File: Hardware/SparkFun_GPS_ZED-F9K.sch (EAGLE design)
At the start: 73 parts, among them J3 QWIIC_RIGHT_ANGLE, J4 QWIIC_RIGHT_ANGLE, U1 DUAL-OPTO_HCPL-073L, U2 U-BLOX_ZED_F9R, U3 UHS_INVERTER_SCHMITT_TRIGGERS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, U4 UHS_INVERTER_SCHMITT_TRIGGERS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, U5 3.3V

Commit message: Updates libraries, replaces F9R with F9K, fixes some text in schematic, deletes blank sheets in schematic
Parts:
- FB1: value 120NH -> 120Ω; device SparkFun-Coils:FERRITE_BEAD_GNSS -> SparkFun-Coils:FERRITE_BEAD-120_OHM-0402
- U1: value DUAL-OPTO_HCPL-073L -> DUAL-OPTO_HCPL-073LSOIC-8; device SparkFun-DiscreteSemi:DUAL-OPTO_HCPL-073L -> SparkFun-DiscreteSemi:DUAL-OPTO_HCPL-073LSOIC-8
- U2: value U-BLOX_ZED_F9R -> U-BLOX_ZED_F9K; device SparkFun-GPS:U-BLOX_ZED_F9R -> f9k:U-BLOX_ZED_F9K
- renumbered JP1 to PWR, JP2 to PPS, JP3 to RTK, JP4 to GEO, JP5 to SPI
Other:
- note added: "GNSS/Dead Reckoning Module - ublox ZED-F9K"
- note removed: "Dead Reckoning Module - ublox ZED-F9R"
- moved on the sheet: C1, C6, C7, R4, R7

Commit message: Updates script being used
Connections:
- net DIR_SCHMITT renamed DIR_INV
- net WT_SCHMITT renamed WT_INV
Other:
- moved on the sheet: C7
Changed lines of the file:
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@@
 <attribute name="VALUE" x="76.2" y="81.534" size="1.778" layer="96" font="vector" align="bottom-center"/>
 </instance>
-<instance part="GND26" gate="1" x="76.2" y="30.48" smashed="yes">
-<attribute name="VALUE" x="76.2" y="30.226" size="1.778" layer="96" font="vector" align="top-center"/>
+<instance part="GND26" gate="1" x="78.74" y="30.48" smashed="yes">
+<attribute name="VALUE" x="78.74" y="30.226" size="1.778" layer="96" font="vector" align="top-center"/>
 </instance>
 <instance part="D1" gate="G$1" x="43.18" y="45.72" smashed="yes" rot="R90">
@@
 <attribute name="VALUE" x="69.85" y="61.341" size="1.778" layer="96" font="vector"/>
 </instance>
-<instance part="C7" gate="G$1" x="76.2" y="40.64" smashed="yes">
-<attribute name="NAME" x="71.374" y="43.561" size="1.778" layer="95" font="vector"/>
-<attribute name="VALUE" x="69.088" y="38.481" size="1.778" layer="96" font="vector"/>
+<instance part="C7" gate="G$1" x="78.74" y="40.64" smashed="yes">
+<attribute name="NAME" x="73.914" y="43.561" size="1.778" layer="95" font="vector"/>
+<attribute name="VALUE" x="71.628" y="38.481" size="1.778" layer="96" font="vector"/>
 </instance>
 <instance part="GND29" gate="1" x="76.2" y="53.34" smashed="yes">
@@
 </segment>
 <segment>
-<wire x1="76.2" y1="38.1" x2="76.2" y2="35.56" width="0.1524" layer="91"/>
-<wire x1="76.2" y1="35.56" x2="76.2" y2="33.02" width="0.1524" layer="91"/>
+<wire x1="78.74" y1="38.1" x2="78.74" y2="35.56" width="0.1524" layer="91"/>
+<wire x1="78.74" y1="35.56" x2="78.74" y2="33.02" width="0.1524" layer="91"/>
 <wire x1="88.9" y1="38.1" x2="88.9" y2="35.56" width="0.1524" layer="91"/>
-<wire x1="88.9" y1="35.56" x2="76.2" y2="35.56" width="0.1524" layer="91"/>
-<junction x="76.2" y="35.56"/>
+<wire x1="88.9" y1="35.56" x2="78.74" y2="35.56" width="0.1524" layer="91"/>
+<junction x="78.74" y="35.56"/>
 <pinref part="GND26" gate="1" pin="GND"/>
 <pinref part="C7" gate="G$1" pin="2"/>
@@
 </segment>
 <segment>
-<wire x1="88.9" y1="71.12" x2="76.2" y2="71.12" width="0.1524" layer="91"/>
-<junction x="88.9" y="71.12"/>
+<wire x1="93.98" y1="71.12" x2="81.28" y2="71.12" width="0.1524" layer="91"/>
+<wire x1="81.28" y1="71.12" x2="76.2" y2="71.12" width="0.1524" layer="91"/>
 <wire x1="76.2" y1="71.12" x2="76.2" y2="68.58" width="0.1524" layer="91"/>
-<wire x1="88.9" y1="48.26" x2="88.9" y2="71.12" width="0.1524" layer="91"/>
-<junction x="88.9" y="71.12"/>
-<wire x1="76.2" y1="45.72" x2="76.2" y2="48.26" width="0.1524" layer="91"/>
-<wire x1="76.2" y1="48.26" x2="88.9" y2="48.26" width="0.1524" layer="91"/>
+<wire x1="78.74" y1="45.72" x2="78.74" y2="48.26" width="0.1524" layer="91"/>
+<wire x1="78.74" y1="48.26" x2="81.28" y2="48.26" width="0.1524" layer="91"/>
 <pinref part="SUPPLY22" gate="G$1" pin="3.3V"/>
 <pinref part="C6" gate="G$1" pin="1"/>
 <pinref part="C7" gate="G$1" pin="1"/>
 <pinref part="U3" gate="U1" pin="VCC"/>
-<wire x1="93.98" y1="71.12" x2="88.9" y2="71.12" width="0.1524" layer="91"/>
+<wire x1="81.28" y1="48.26" x2="93.98" y2="48.26" width="0.1524" layer="91"/>
 <wire x1="76.2" y1="78.74" x2="76.2" y2="71.12" width="0.1524" layer="91"/>
 <junction x="76.2" y="71.12"/>
 <pinref part="U4" gate="U1" pin="VCC"/>
-<wire x1="93.98" y1="48.26" x2="88.9" y2="48.26" width="0.1524" layer="91"/>
-<junction x="88.9" y="48.26"/>
+<wire x1="81.28" y1="48.26" x2="81.28" y2="71.12" width="0.1524" layer="91"/>
+<junction x="81.28" y="48.26"/>
+<junction x="81.28" y="71.12"/>
 </segment>
 <segment>
@@
 </segment>
 </net>
-<net name="WT_SCHMITT" class="0">
+<net name="WT_INV" class="0">
 <segment>
 <pinref part="R7" gate="G$1" pin="1"/>
@@
 </segment>
 </net>
-<net name="DIR_SCHMITT" class="0">
+<net name="DIR_INV" class="0">
 <segment>
 <pinref part="R4" gate="G$1" pin="1"/>

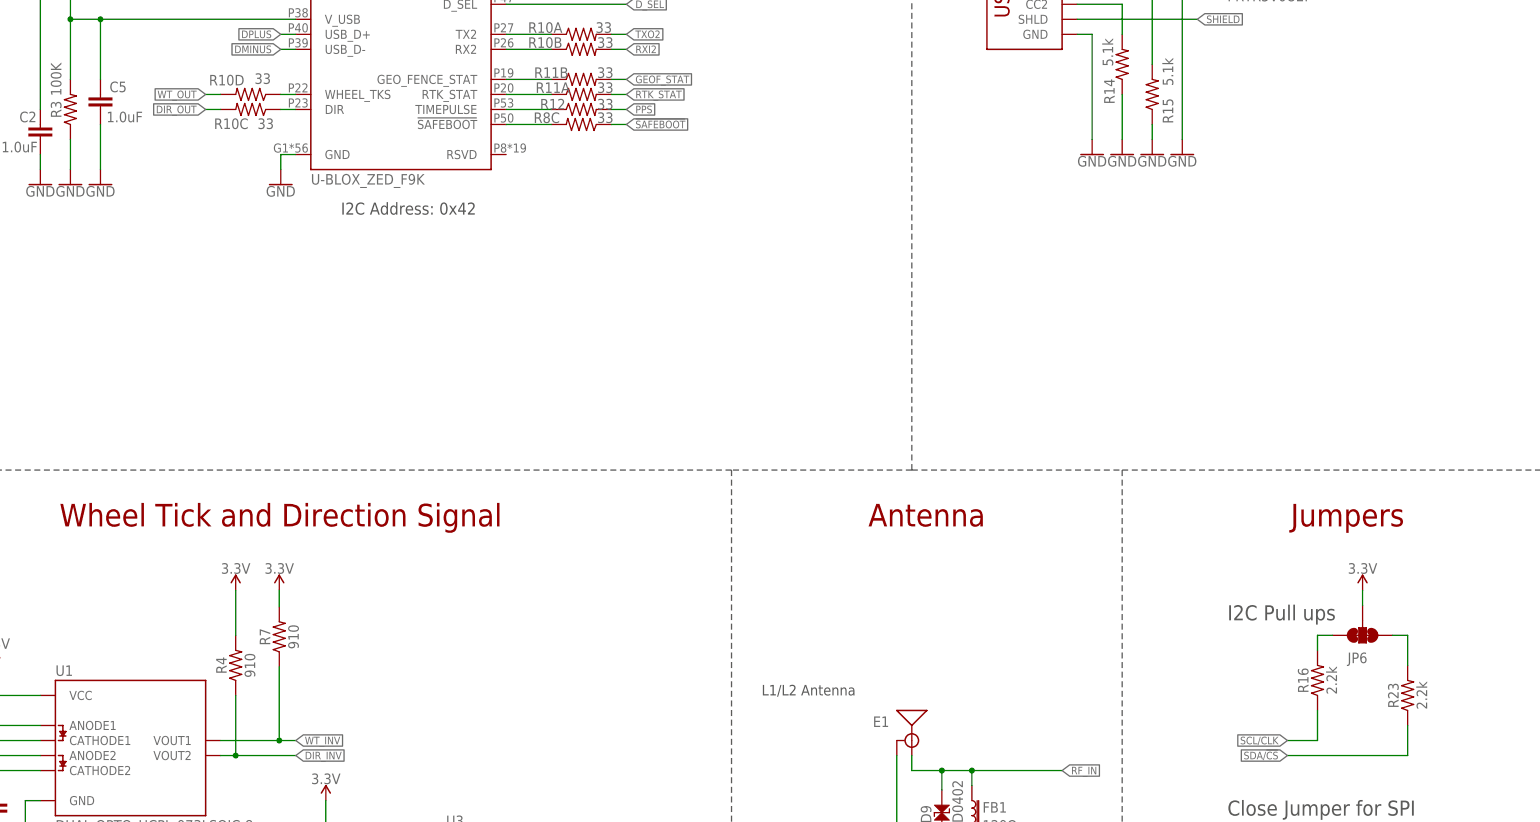
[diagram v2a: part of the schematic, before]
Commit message: Moves traces for better ground pour and to reduce cross talk
* Replaces all capacitors with smaller footprint
* Replaces 2.2K resistors with 4.7K resistors
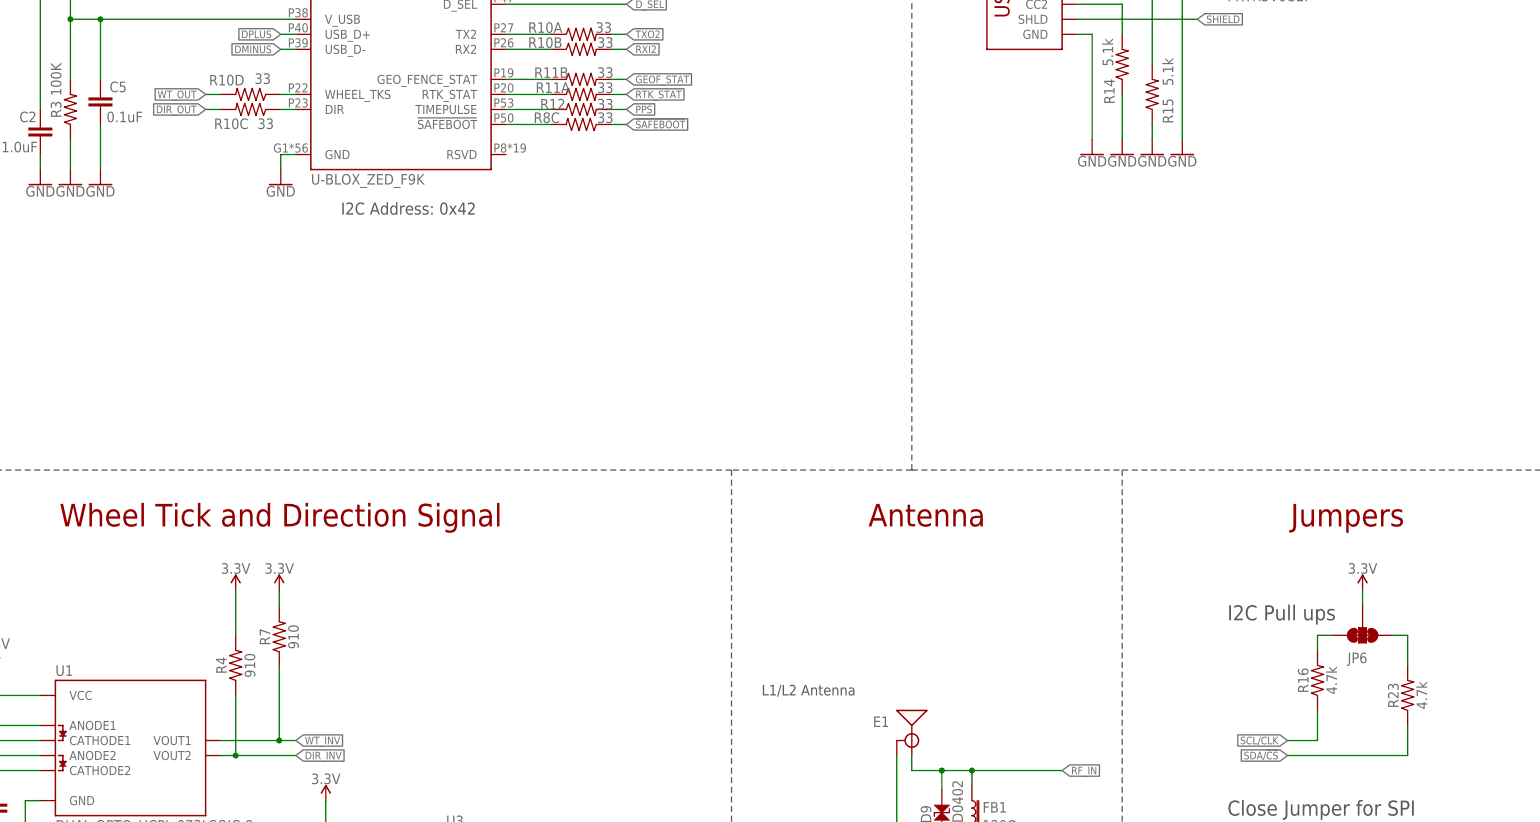
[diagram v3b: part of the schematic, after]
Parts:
- C1, C6, C7: device SparkFun-Capacitors:0.1UF-0402-10V-10%-X7R -> SparkFun-Capacitors:0.1UF-0402T-6.3V-10%-X7R
- C10, C2, C9: device SparkFun-Capacitors:1.0UF-0603-16V-10%-X7R -> SparkFun-Capacitors:1.0UF-0402T-16V-10%
- C5: value 1.0uF -> 0.1uF; device SparkFun-Capacitors:1.0UF-0603-16V-10%-X7R -> SparkFun-Capacitors:0.1UF-0402T-6.3V-10%-X7R
- R16, R23: value 2.2k -> 4.7k; device SparkFun-Resistors:2.2KOHM-0603-1/10W-1% -> SparkFun-Resistors:4.7KOHM-0402T-1/16W-1%
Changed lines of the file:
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@@
 <?xml version="1.0" encoding="utf-8"?>
 <!DOCTYPE eagle SYSTEM "eagle.dtd">
-<eagle version="9.6.2">
+<eagle version="9.5.1">
 <drawing>
 <settings>
@@
 <parts>
 <part name="J3" library="SparkFun-Connectors" deviceset="QWIIC_CONNECTOR" device="JS-1MM" value="QWIIC_RIGHT_ANGLE"/>
-<part name="R23" library="SparkFun-Resistors" deviceset="2.2KOHM" device="-0603-1/10W-1%" value="2.2k"/>
-<part name="R16" library="SparkFun-Resistors" deviceset="2.2KOHM" device="-0603-1/10W-1%" value="2.2k"/>
+<part name="R23" library="SparkFun-Resistors" deviceset="4.7KOHM" device="-0402T-1/16W-1%" value="4.7k"/>
+<part name="R16" library="SparkFun-Resistors" deviceset="4.7KOHM" device="-0402T-1/16W-1%" value="4.7k"/>
 <part name="JP6" library="SparkFun-Jumpers" deviceset="JUMPER-SMT_3_2-NC_TRACE" device="_SILK" package3d_urn="urn:adsk.eagle:package:39289/1"/>
 <part name="GND12" library="SparkFun-PowerSymbols" deviceset="GND" device=""/>
@@
 <part name="GND15" library="SparkFun-PowerSymbols" deviceset="GND" device=""/>
 <part name="SUPPLY11" library="SparkFun-PowerSymbols" deviceset="3.3V" device=""/>
-<part name="C9" library="SparkFun-Capacitors" deviceset="1.0UF" device="-0603-16V-10%-X7R" value="1.0uF"/>
-<part name="C10" library="SparkFun-Capacitors" deviceset="1.0UF" device="-0603-16V-10%-X7R" value="1.0uF"/>
+<part name="C9" library="SparkFun-Capacitors" deviceset="1.0UF" device="-0402T-16V-10%" value="1.0uF"/>
+<part name="C10" library="SparkFun-Capacitors" deviceset="1.0UF" device="-0402T-16V-10%" value="1.0uF"/>
 <part name="GND14" library="SparkFun-PowerSymbols" deviceset="GND" device=""/>
 <part name="GND17" library="SparkFun-PowerSymbols" deviceset="GND" device=""/>
@@
 <part name="SUPPLY1" library="SparkFun-PowerSymbols" deviceset="V_BATT" device=""/>
 <part name="U2" library="f9k" deviceset="U-BLOX_ZED_F9K" device=""/>
-<part name="C2" library="SparkFun-Capacitors" deviceset="1.0UF" device="-0603-16V-10%-X7R" value="1.0uF"/>
+<part name="C2" library="SparkFun-Capacitors" deviceset="1.0UF" device="-0402T-16V-10%" value="1.0uF"/>
 <part name="SUPPLY3" library="SparkFun-PowerSymbols" deviceset="3.3V" device=""/>
 <part name="R3" library="SparkFun-Resistors" deviceset="100KOHM" device="-0402-1/16W-1%" value="100K"/>
@@
 <part name="R4" library="SparkFun-Resistors" deviceset="910OHM" device="-0603-1/10W-5%" value="910"/>
 <part name="U1" library="SparkFun-DiscreteSemi" deviceset="DUAL-OPTO_HCPL-073L" device="SOIC-8"/>
-<part name="C1" library="SparkFun-Capacitors" deviceset="0.1UF" device="-0402-10V-10%-X7R" value="0.1uF"/>
+<part name="C1" library="SparkFun-Capacitors" deviceset="0.1UF" device="-0402T-6.3V-10%-X7R" value="0.1uF"/>
 <part name="SUPPLY21" library="SparkFun-PowerSymbols" deviceset="3.3V" device=""/>
 <part name="GND25" library="SparkFun-PowerSymbols" deviceset="GND" device=""/>
@@
 <part name="SUPPLY23" library="SparkFun-PowerSymbols" deviceset="3.3V" device=""/>
 <part name="SUPPLY24" library="SparkFun-PowerSymbols" deviceset="3.3V" device=""/>
-<part name="C6" library="SparkFun-Capacitors" deviceset="0.1UF" device="-0402-10V-10%-X7R" value="0.1uF"/>
-<part name="C7" library="SparkFun-Capacitors" deviceset="0.1UF" device="-0402-10V-10%-X7R" value="0.1uF"/>
+<part name="C6" library="SparkFun-Capacitors" deviceset="0.1UF" device="-0402T-6.3V-10%-X7R" value="0.1uF"/>
+<part name="C7" library="SparkFun-Capacitors" deviceset="0.1UF" device="-0402T-6.3V-10%-X7R" value="0.1uF"/>
 <part name="GND29" library="SparkFun-PowerSymbols" deviceset="GND" device=""/>
-<part name="C5" library="SparkFun-Capacitors" deviceset="1.0UF" device="-0603-16V-10%-X7R" value="1.0uF"/>
+<part name="C5" library="SparkFun-Capacitors" deviceset="0.1UF" device="-0402T-6.3V-10%-X7R" value="0.1uF"/>
 <part name="GND20" library="SparkFun-PowerSymbols" deviceset="GND" device=""/>
 <part name="GND21" library="SparkFun-PowerSymbols" deviceset="GND" device=""/>

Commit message: Flips FTDI header, adds testpoint for VBAT, fixes dimension line width
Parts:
- added TP1: TEST-POINT3X5, SparkFun-Connectors:TEST-POINT3X5
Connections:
- net GND: now also J7.6; no longer J7.1
- net RXI2: now also J7.3; no longer J7.4
- net TXO2: now also J7.2; no longer J7.5
- net V_BATT: now also TP1.1
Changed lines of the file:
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@@
 <?xml version="1.0" encoding="utf-8"?>
 <!DOCTYPE eagle SYSTEM "eagle.dtd">
-<eagle version="9.5.1">
+<eagle version="9.6.2">
 <drawing>
 <settings>
@@
 <part name="U3" library="SparkFun-IC-Amplifiers" deviceset="UHS_INVERTER_SCHMITT_TRIGGER" device="SIP6" value="UHS_INVERTER_SCHMITT_TRIGGERSIP6"/>
 <part name="U4" library="SparkFun-IC-Amplifiers" deviceset="UHS_INVERTER_SCHMITT_TRIGGER" device="SIP6" value="UHS_INVERTER_SCHMITT_TRIGGERSIP6"/>
+<part name="TP1" library="SparkFun-Connectors" deviceset="TEST-POINT" device="3X5"/>
 </parts>
 <sheets>
@@
 <attribute name="VALUE" x="96.52" y="33.02" size="1.778" layer="95"/>
 </instance>
+<instance part="TP1" gate="G$1" x="391.16" y="208.28" smashed="yes">
+<attribute name="NAME" x="391.16" y="210.82" size="1.778" layer="95" font="vector"/>
+</instance>
 </instances>
 <busses>
@@
 </segment>
 <segment>
-<pinref part="J7" gate="G$1" pin="1"/>
-<wire x1="391.16" y1="86.36" x2="393.7" y2="86.36" width="0.1524" layer="91"/>
-<wire x1="393.7" y1="86.36" x2="393.7" y2="68.58" width="0.1524" layer="91"/>
 <pinref part="GND18" gate="1" pin="GND"/>
-<wire x1="393.7" y1="114.3" x2="393.7" y2="86.36" width="0.1524" layer="91"/>
-<junction x="393.7" y="86.36"/>
+<wire x1="393.7" y1="73.66" x2="393.7" y2="68.58" width="0.1524" layer="91"/>
+<wire x1="393.7" y1="114.3" x2="393.7" y2="73.66" width="0.1524" layer="91"/>
 <pinref part="J6" gate="J1" pin="9"/>
 <wire x1="391.16" y1="114.3" x2="393.7" y2="114.3" width="0.1524" layer="91"/>
+<pinref part="J7" gate="G$1" pin="6"/>
+<wire x1="391.16" y1="73.66" x2="393.7" y2="73.66" width="0.1524" layer="91"/>
+<junction x="393.7" y="73.66"/>
 </segment>
 <segment>
@@
 <wire x1="388.62" y1="208.28" x2="388.62" y2="233.68" width="0.1524" layer="91"/>
 <pinref part="BT1" gate="G$1" pin="+"/>
+<wire x1="391.16" y1="208.28" x2="388.62" y2="208.28" width="0.1524" layer="91"/>
+<junction x="388.62" y="208.28"/>
+<pinref part="TP1" gate="G$1" pin="1"/>
 </segment>
 <segment>
@@
 <net name="TXO2" class="0">
 <segment>
-<pinref part="J7" gate="G$1" pin="5"/>
-<wire x1="391.16" y1="76.2" x2="396.24" y2="76.2" width="0.1524" layer="91"/>
-<label x="396.24" y="76.2" size="1.27" layer="95" font="vector" xref="yes"/>
-</segment>
-<segment>
 <wire x1="124.46" y1="208.28" x2="127" y2="208.28" width="0.1524" layer="91"/>
 <label x="127" y="208.28" size="1.27" layer="95" font="vector" xref="yes"/>
 <pinref part="R10" gate="A" pin="2"/>
 </segment>
+<segment>
+<pinref part="J7" gate="G$1" pin="2"/>
+<wire x1="391.16" y1="83.82" x2="396.24" y2="83.82" width="0.1524" layer="91"/>
+<label x="396.24" y="83.82" size="1.27" layer="95" font="vector" xref="yes"/>
+</segment>
 </net>
 <net name="RXI2" class="0">
-<segment>
-<pinref part="J7" gate="G$1" pin="4"/>
-<wire x1="391.16" y1="78.74" x2="396.24" y2="78.74" width="0.1524" layer="91"/>
-<label x="396.24" y="78.74" size="1.27" layer="95" font="vector" xref="yes"/>
-</segment>
 <segment>
 <wire x1="124.46" y1="205.74" x2="127" y2="205.74" width="0.1524" layer="91"/>
@@
 <pinref part="R10" gate="B" pin="2"/>
 </segment>
-</net>
+<segment>
+<pinref part="J7" gate="G$1" pin="3"/>
+<wire x1="391.16" y1="81.28" x2="396.24" y2="81.28" width="0.1524" layer="91"/>
+<label x="396.24" y="81.28" size="1.27" layer="95" font="vector" xref="yes"/>
+</segment>
+</net>
